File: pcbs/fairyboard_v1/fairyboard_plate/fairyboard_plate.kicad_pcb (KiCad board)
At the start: 2 copper layers, 130 x 118.5 mm, 7 parts

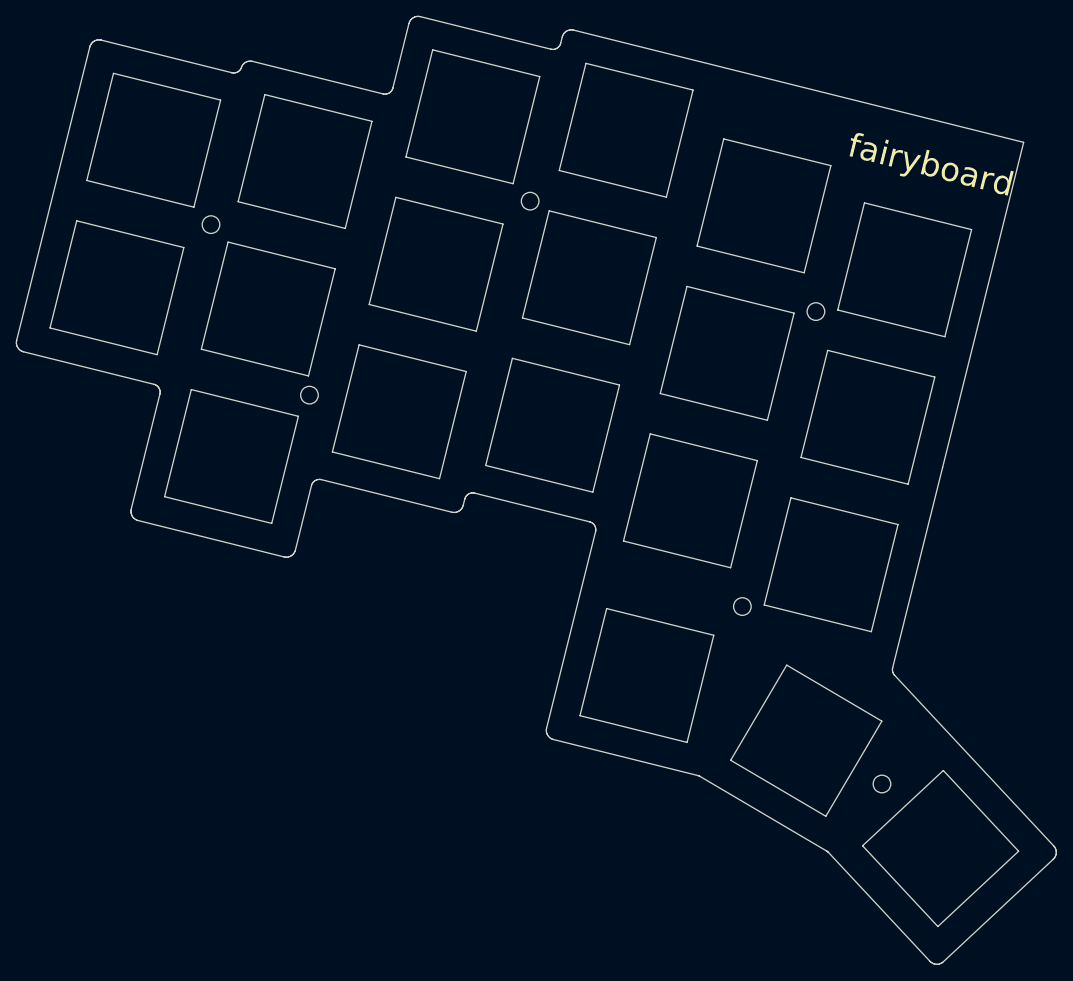
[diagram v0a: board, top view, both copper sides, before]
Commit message: feat: updated holes of pcb plate to be 2.4mm diameter instead of 2.2
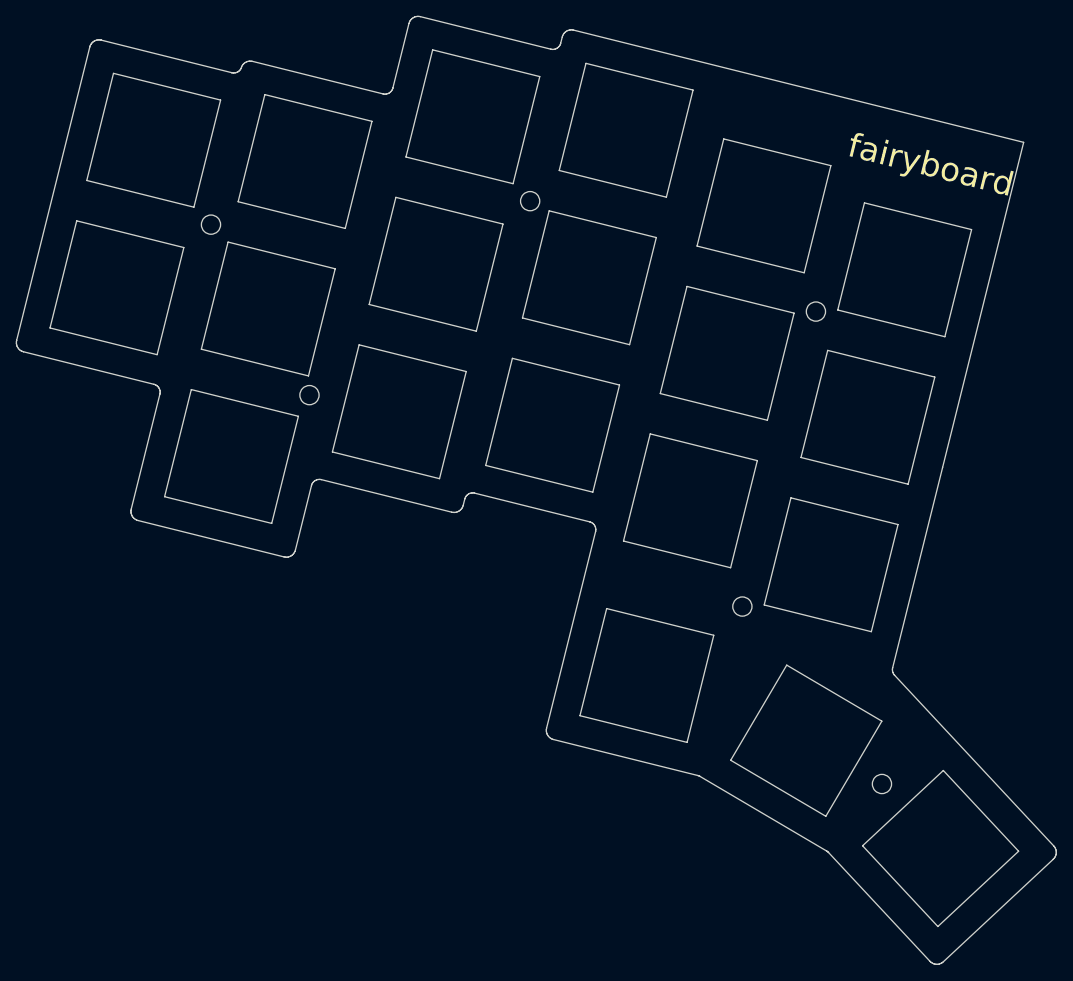
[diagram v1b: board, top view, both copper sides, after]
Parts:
- REF** (x6): value MountingHole_2.2mm_M2 -> MountingHole_2.4mm_M2
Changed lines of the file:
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@@
 			(drillshape 0)
 			(scaleselection 1)
-			(outputdirectory "")
+			(outputdirectory "fabrication/")
 		)
 	)
@@
 			)
 		)
-		(property "Value" "MountingHole_2.2mm_M2"
+		(property "Value" "MountingHole_2.4mm_M2"
 			(at 0 3.15 0)
 			(layer "F.Fab")
@@
 		(pad "" np_thru_hole circle
 			(at 0 0)
-			(size 2.2 2.2)
-			(drill 2.2)
+			(size 2.4 2.4)
+			(drill 2.4)
 			(layers "*.Cu" "*.Mask")
 		)
@@
 			)
 		)
-		(property "Value" "MountingHole_2.2mm_M2"
+		(property "Value" "MountingHole_2.4mm_M2"
 			(at 0 3.15 0)
 			(layer "F.Fab")
@@
 		(pad "" np_thru_hole circle
 			(at 0 0)
-			(size 2.2 2.2)
-			(drill 2.2)
+			(size 2.4 2.4)
+			(drill 2.4)
 			(layers "*.Cu" "*.Mask")
 		)
@@
 			)
 		)
-		(property "Value" "MountingHole_2.2mm_M2"
+		(property "Value" "MountingHole_2.4mm_M2"
 			(at 0 3.15 0)
 			(layer "F.Fab")
@@
 		(pad "" np_thru_hole circle
 			(at 0 0)
-			(size 2.2 2.2)
-			(drill 2.2)
+			(size 2.4 2.4)
+			(drill 2.4)
 			(layers "*.Cu" "*.Mask")
 		)
@@
 			)
 		)
-		(property "Value" "MountingHole_2.2mm_M2"
+		(property "Value" "MountingHole_2.4mm_M2"
 			(at 0 3.15 0)
 			(layer "F.Fab")
@@
 		(pad "" np_thru_hole circle
 			(at 0 0)
-			(size 2.2 2.2)
-			(drill 2.2)
+			(size 2.4 2.4)
+			(drill 2.4)
 			(layers "*.Cu" "*.Mask")
 		)
@@
 			)
 		)
-		(property "Value" "MountingHole_2.2mm_M2"
+		(property "Value" "MountingHole_2.4mm_M2"
 			(at 0 3.15 0)
 			(layer "F.Fab")
@@
 		(pad "" np_thru_hole circle
 			(at 0 0)
-			(size 2.2 2.2)
-			(drill 2.2)
+			(size 2.4 2.4)
+			(drill 2.4)
 			(layers "*.Cu" "*.Mask")
 		)
@@
 			)
 		)
-		(property "Value" "MountingHole_2.2mm_M2"
+		(property "Value" "MountingHole_2.4mm_M2"
 			(at 0 3.15 0)
 			(layer "F.Fab")
@@
 		(pad "" np_thru_hole circle
 			(at 0 0)
-			(size 2.2 2.2)
-			(drill 2.2)
+			(size 2.4 2.4)
+			(drill 2.4)
 			(layers "*.Cu" "*.Mask")
 		)
